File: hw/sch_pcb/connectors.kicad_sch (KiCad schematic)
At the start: 8 parts, among them J2 3.3-5V, J3 JUMP_5X2, J4 JUMP_5X2, U1 TXS0104EPW, U3 TXS0104EPW

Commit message: Update project workflows.
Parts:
- J2: symbol MLAB_Jumpers:JUMP_3X2 -> MLAB_HEADER:HEADER_2x03_PARALLEL
- J3, J4: symbol MLAB_Jumpers:JUMP_5X2 -> MLAB_HEADER:HEADER_2x04_PARALLEL
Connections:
- net at J3.1, J3.2: now also U3.10 (B4)
- net at J3.3, J3.4: now also U3.11 (B3); no longer U3.10 (B4)
- net at J3.5, J3.6: now also U3.12 (B2); no longer U3.11 (B3)
- net at J3.7, J3.8: now also U3.13 (B1); no longer U3.12 (B2)
- net at J4.1, J4.2: now also U1.10 (B4)
- net at J4.3, J4.4: now also U1.11 (B3); no longer U1.10 (B4)
- net at J4.5, J4.6: now also U1.12 (B2); no longer U1.11 (B3)
- net at J4.7, J4.8: now also U1.13 (B1); no longer U1.12 (B2)
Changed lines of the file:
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@@
 	)
 	(symbol
-		(lib_id "MLAB_Jumpers:JUMP_5X2")
-		(at 46.99 85.09 180)
+		(lib_id "MLAB_HEADER:HEADER_2x04_PARALLEL")
+		(at 50.8 82.55 180)
 		(unit 1)
 		(exclude_from_sim no)
@@
 		(fields_autoplaced yes)
 		(property "Reference" "J3"
-			(at 49.53 73.66 0)
+			(at 50.8 73.0439 0)
 			(effects
 				(font
@@
 		)
 		(property "Value" "JUMP_5X2"
-			(at 48.26 83.82 90)
+			(at 52.07 81.28 90)
 			(effects
 				(font
@@
 		)
 		(property "Footprint" "Mlab_Pin_Headers:Straight_2x05"
-			(at 49.53 76.2 0)
-			(effects
-				(font
-					(size 1.524 1.524)
-				)
+			(at 50.8 75.6725 0)
+			(effects
+				(font
+					(size 1.524 1.524)
+				)
+				(hide yes)
 			)
 		)
 		(property "Datasheet" ""
-			(at 46.99 85.09 0)
-			(effects
-				(font
-					(size 1.524 1.524)
-				)
-			)
-		)
-		(property "Description" "MLAB modified doubled pinheader connector"
-			(at 46.99 85.09 0)
-			(effects
-				(font
-					(size 1.27 1.27)
-				)
-				(hide yes)
-			)
-		)
-		(pin "9"
+			(at 50.8 86.36 0)
+			(effects
+				(font
+					(size 1.524 1.524)
+				)
+			)
+		)
+		(property "Description" "2x04 2.54 mm pitch header, 2 pins next to each other are connected"
+			(at 50.8 82.55 0)
+			(effects
+				(font
+					(size 1.27 1.27)
+				)
+				(hide yes)
+			)
+		)
+		(property "UST_ID" ""
+			(at 50.8 82.55 0)
+			(effects
+				(font
+					(size 1.27 1.27)
+				)
+				(hide yes)
+			)
 		)
 		(pin "3"
@@
 		)
 		(pin "7"
-		)
-		(pin "10"
 		)
 		(instances
@@
 	)
 	(symbol
-		(lib_id "MLAB_Jumpers:JUMP_5X2")
-		(at 46.99 132.08 180)
+		(lib_id "MLAB_HEADER:HEADER_2x04_PARALLEL")
+		(at 50.8 129.54 180)
 		(unit 1)
 		(exclude_from_sim no)
@@
 		(fields_autoplaced yes)
 		(property "Reference" "J4"
-			(at 49.53 120.65 0)
+			(at 50.8 120.0339 0)
 			(effects
 				(font
@@
 		)
 		(property "Value" "JUMP_5X2"
-			(at 48.26 130.81 90)
+			(at 52.07 128.27 90)
 			(effects
 				(font
@@
 		)
 		(property "Footprint" "Mlab_Pin_Headers:Straight_2x05"
-			(at 49.53 123.19 0)
-			(effects
-				(font
-					(size 1.524 1.524)
-				)
+			(at 50.8 122.6625 0)
+			(effects
+				(font
+					(size 1.524 1.524)
+				)
+				(hide yes)
 			)
 		)
 		(property "Datasheet" ""
-			(at 46.99 132.08 0)
-			(effects
-				(font
-					(size 1.524 1.524)
-				)
-			)
-		)
-		(property "Description" "MLAB modified doubled pinheader connector"
-			(at 46.99 132.08 0)
-			(effects
-				(font
-					(size 1.27 1.27)
-				)
-				(hide yes)
-			)
-		)
-		(pin "9"
+			(at 50.8 133.35 0)
+			(effects
+				(font
+					(size 1.524 1.524)
+				)
+			)
+		)
+		(property "Description" "2x04 2.54 mm pitch header, 2 pins next to each other are connected"
+			(at 50.8 129.54 0)
+			(effects
+				(font
+					(size 1.27 1.27)
+				)
+				(hide yes)
+			)
+		)
+		(property "UST_ID" ""
+			(at 50.8 129.54 0)
+			(effects
+				(font
+					(size 1.27 1.27)
+				)
+				(hide yes)
+			)
 		)
 		(pin "3"
@@
 		)
 		(pin "7"
-		)
-		(pin "10"
 		)
 		(instances
@@
 	)
 	(symbol
-		(lib_id "MLAB_Jumpers:JUMP_3X2")
-		(at 45.72 39.37 0)
+		(lib_id "MLAB_HEADER:HEADER_2x03_PARALLEL")
+		(at 49.53 38.1 0)
 		(mirror y)
 		(unit 1)
@@
 		(dnp no)
 		(property "Reference" "J2"
-			(at 47.498 42.418 0)
+			(at 51.308 41.148 0)
 			(effects
 				(font
@@
 		)
 		(property "Value" "3.3-5V"
-			(at 49.022 32.766 0)
+			(at 52.832 31.496 0)
 			(effects
 				(font
@@
 		)
 		(property "Footprint" "Mlab_Pin_Headers:Straight_2x03"
-			(at 45.72 39.37 0)
+			(at 49.53 35.56 0)
 			(effects
 				(font
@@
 		)
 		(property "Datasheet" ""
-			(at 45.72 39.37 0)
-			(effects
-				(font
-					(size 1.524 1.524)
-				)
-			)
-		)
-		(property "Description" "MLAB modified doubled pinheader connector"
-			(at 45.72 39.37 0)
-			(effects
-				(font
+			(at 49.53 35.56 0)
+			(effects
+				(font
+					(size 1.524 1.524)
+				)
+			)
+		)
+		(property "Description" "2x03 2.54 mm pitch header, 2 pins next to each other are connected"
+			(at 49.53 38.1 0)
+			(effects
+				(font
+					(size 1.27 1.27)
+				)
+				(hide yes)
+			)
+		)
+		(property "UST_ID" ""
+			(at 49.53 38.1 0)
+			(effects
+				(font

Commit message: Fix footprint of pin-headers.
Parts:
- J3, J4: footprint Mlab_Pin_Headers:Straight_2x05 -> Mlab_Pin_Headers:Straight_2x04
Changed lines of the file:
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@@
 			)
 		)
-		(property "Footprint" "Mlab_Pin_Headers:Straight_2x05"
+		(property "Footprint" "Mlab_Pin_Headers:Straight_2x04"
 			(at 50.8 75.6725 0)
 			(effects
@@
 			)
 		)
-		(property "Footprint" "Mlab_Pin_Headers:Straight_2x05"
+		(property "Footprint" "Mlab_Pin_Headers:Straight_2x04"
 			(at 50.8 122.6625 0)
 			(effects

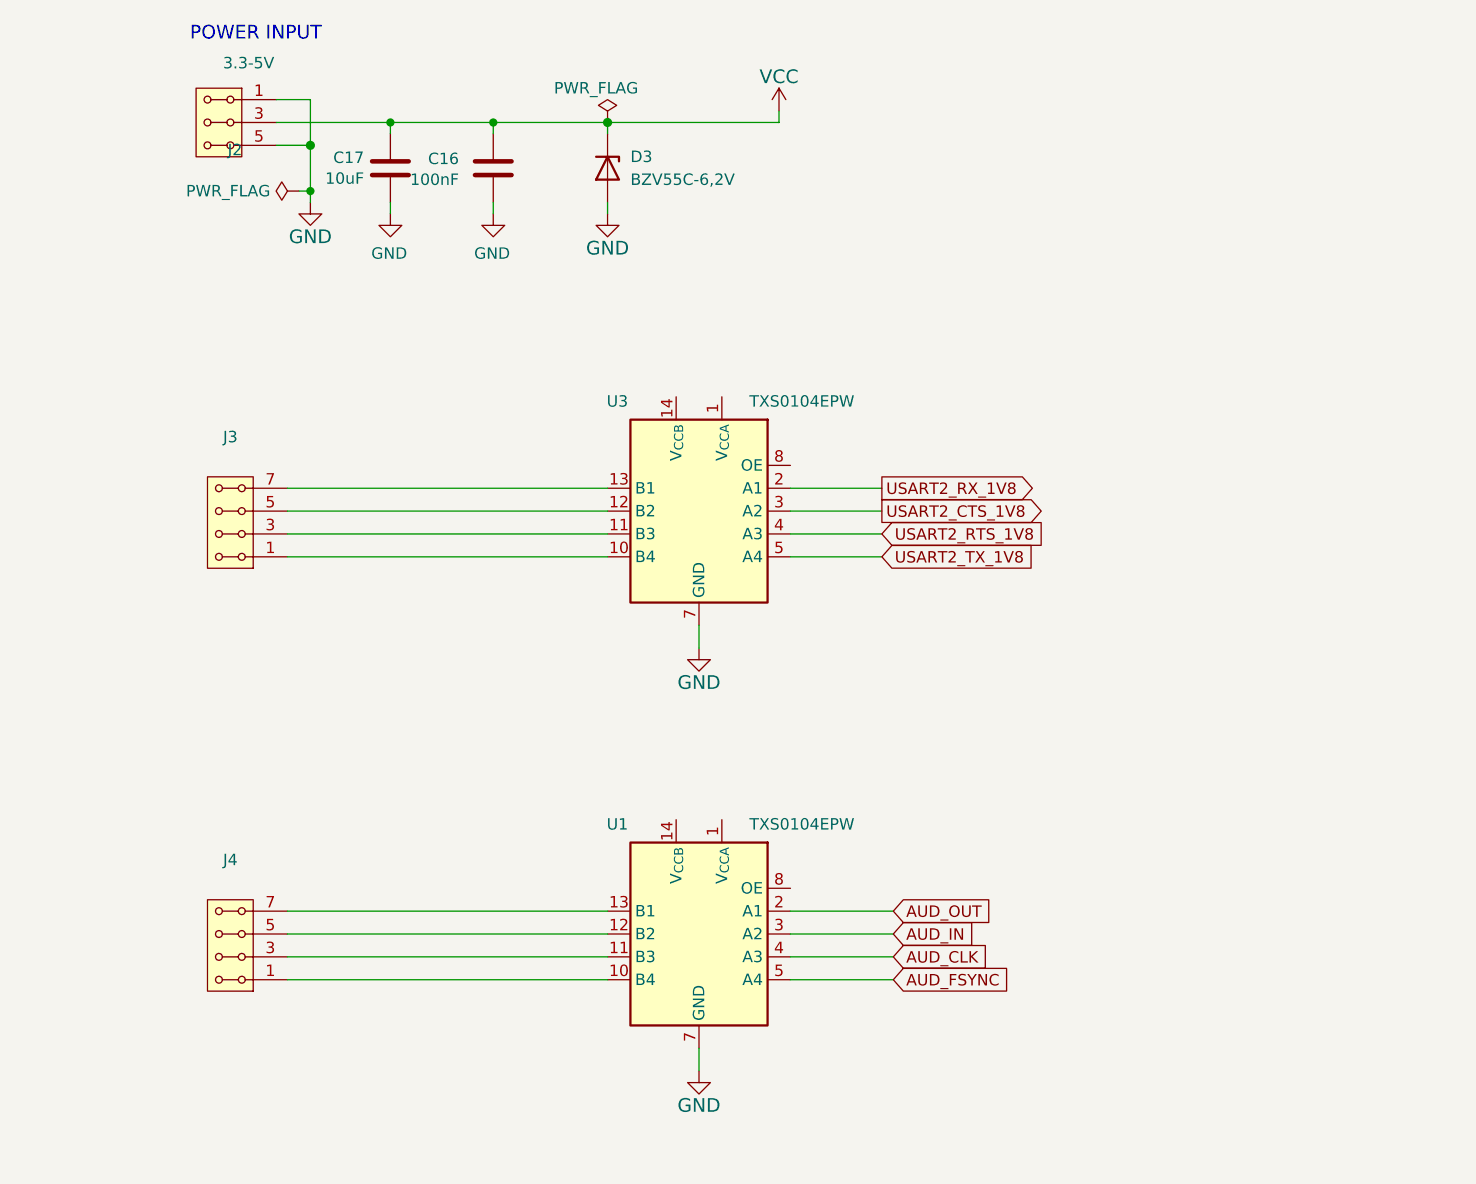
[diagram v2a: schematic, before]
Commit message: Add text for connectors
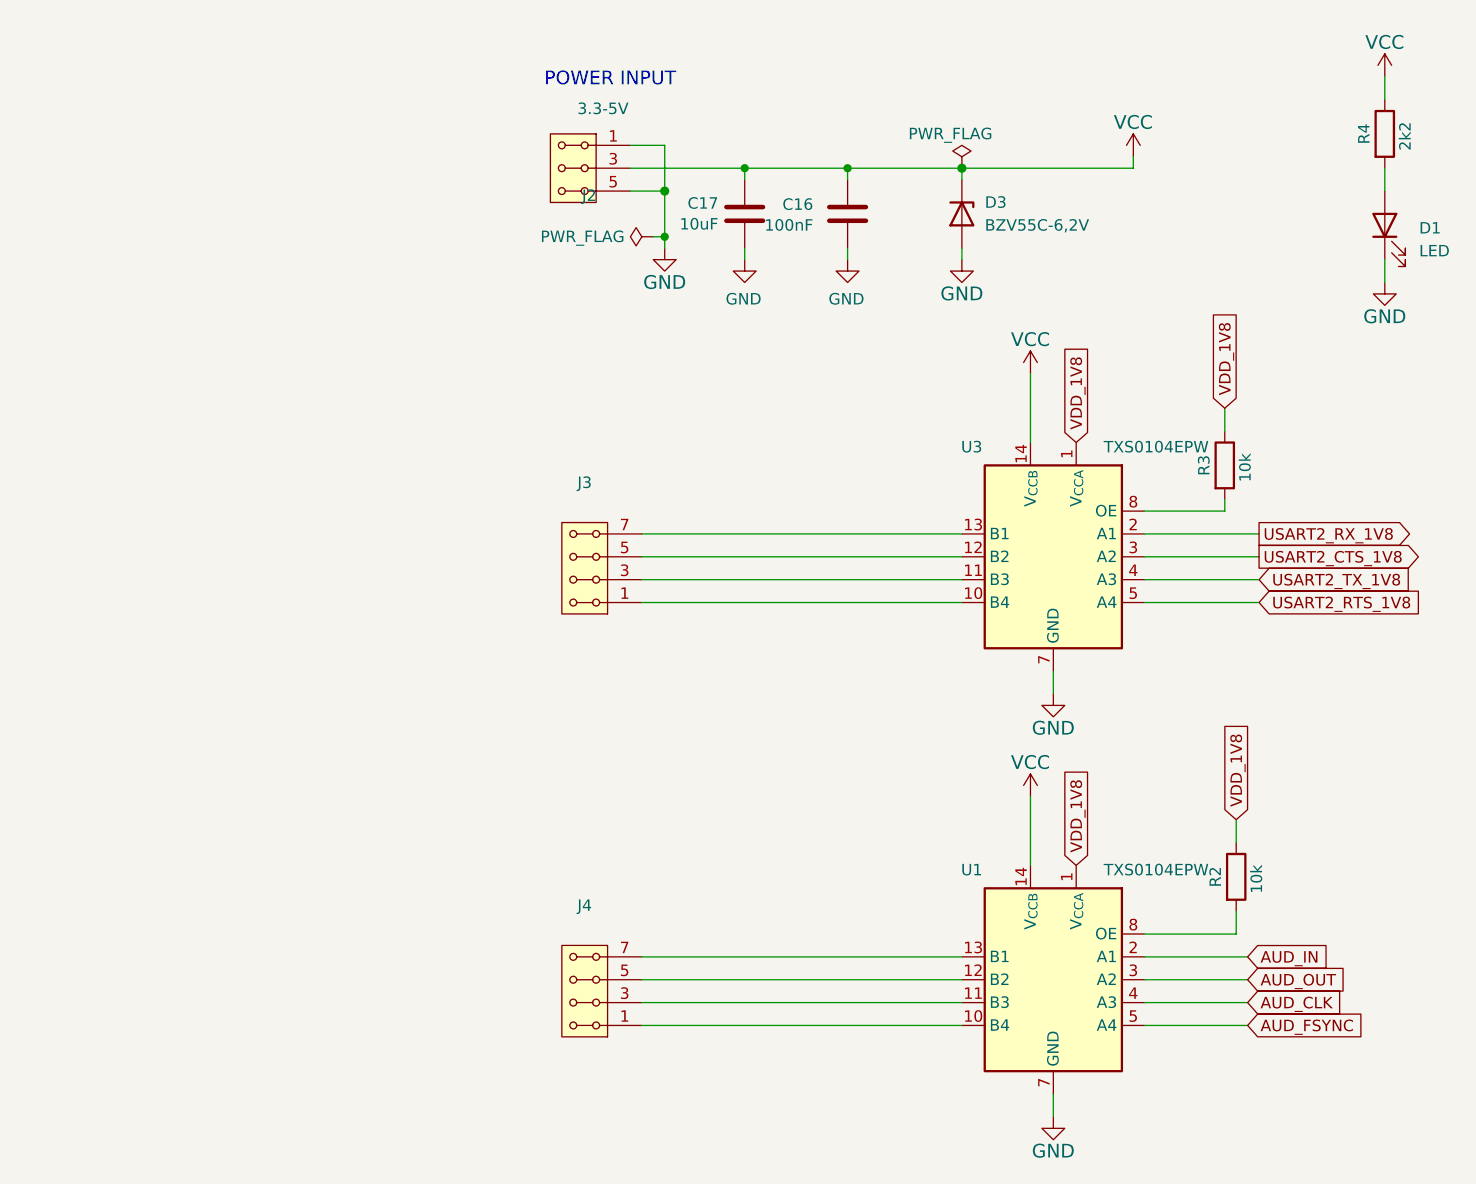
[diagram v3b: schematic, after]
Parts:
- added D1: LED, LED_SMD:LED_0805_2012Metric, symbol Device:LED
- added R2, R3: 10k, Resistor_SMD:R_0603_1608Metric, symbol cc2564-board-rescue:R-Device
- added R4: 2k2, Resistor_SMD:R_0603_1608Metric, symbol cc2564-board-rescue:R-Device
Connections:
- net AUD_IN: now also U1.2 (A1); no longer U1.3 (A2)
- net AUD_OUT: now also U1.3 (A2); no longer U1.2 (A1)
- net GND: now also D1.1 (K)
- net USART2_RTS_1V8: now also U3.5 (A4); no longer U3.4 (A3)
- net USART2_TX_1V8: now also U3.4 (A3); no longer U3.5 (A4)
- net VCC: now also U1.14 (V_{CCB}), U3.14 (V_{CCB}), R4.1
- net VDD_1V8: now reaches U1.1 (V_{CCA})
- net VDD_1V8: now also U3.1 (V_{CCA}), R2.1, R3.1
- net at U1.8 (OE): now also R2.2
- net at U3.8 (OE): now also R3.2
- new net: D1.2 (A), R4.2
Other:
- moved on the sheet: C16, C17, D3, J2, J3, J4, U1, U3

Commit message: Cleanup layout. Fix obsolete part types.
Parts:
- D1: footprint LED_SMD:LED_0805_2012Metric -> Mlab_D:LED_1206_mill
- D3: value BZV55C-6,2V -> BZX585-B5V6.115; footprint Diode_SMD:D_MiniMELF -> Diode_SMD:D_SOD-523; UST_ID 604b0326128750769e5b0f93 -> 60879d38128750769ee58e48
- J2: value 3.3-5V -> 3.3V
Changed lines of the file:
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@@
 		(dnp no)
 		(property "Reference" "C16"
-			(at 115.57 47.2186 0)
+			(at 125.73 45.72 0)
 			(effects
 				(font
@@
 		)
 		(property "Value" "100nF"
-			(at 115.57 49.53 0)
+			(at 127 50.8 0)
 			(effects
 				(font
@@
 			)
 		)
-		(property "Footprint" "LED_SMD:LED_0805_2012Metric"
+		(property "Footprint" "Mlab_D:LED_1206_mill"
 			(at 179.07 49.53 0)
 			(effects
@@
 			)
 		)
+		(property "UST_ID" ""
+			(at 179.07 49.53 0)
+			(effects
+				(font
+					(size 1.27 1.27)
+				)
+				(hide yes)
+			)
+		)
 		(pin "2"
 		)
@@
 			)
 		)
-		(property "Value" "BZV55C-6,2V"
+		(property "Value" "BZX585-B5V6.115"
 			(at 134.62 49.5299 90)
 			(effects
@@
 			)
 		)
-		(property "Footprint" "Diode_SMD:D_MiniMELF"
+		(property "Footprint" "Diode_SMD:D_SOD-523"
 			(at 132.08 48.26 0)
 			(effects
@@
 			)
 		)
-		(property "Datasheet" "~"
+		(property "Datasheet" "https://www.tme.eu/Document/7f59fc987b8fce7e4ab18399d6e66bd1/BZX585-DTE.pdf"
 			(at 132.08 48.26 0)
 			(effects
@@
 			)
 		)
-		(property "UST_ID" "604b0326128750769e5b0f93"
+		(property "UST_ID" "60879d38128750769ee58e48"
 			(at 132.08 48.26 0)
 			(effects
@@
 		(dnp no)
 		(property "Reference" "J2"
-			(at 90.678 46.228 0)
-			(effects
-				(font
-					(size 1.27 1.27)
-				)
-			)
-		)
-		(property "Value" "3.3-5V"
+			(at 83.82 43.18 0)
+			(effects
+				(font
+					(size 1.27 1.27)
+				)
+			)
+		)
+		(property "Value" "3.3V"
 			(at 92.202 36.576 0)
 			(effects

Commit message: Update UST_IDs.
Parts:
- C16: UST_ID 5c70984712875079b91f8b4c -> 5c70984812875079b91f8bf2
- D1: UST_ID (none) -> 64ab2ec176c82a1d3b57875b
- R2, R3: UST_ID (none) -> 5c70984512875079b91f8962
- R4: UST_ID (none) -> 5c70984512875079b91f895e
- U1, U3: UST_ID (none) -> 6998b3d2d42e6e3c4d330d92
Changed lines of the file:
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@@
+			)
+		)
+		(property "UST_ID" "5c70984512875079b91f895e"
+			(at 179.07 39.37 90)
+			(effects
+				(font
+					(size 1.27 1.27)
+				)
+				(hide yes)
 			)
 		)
@@
 			)
 		)
-		(property "UST_ID" "5c70984712875079b91f8b4c"
+		(property "UST_ID" "5c70984812875079b91f8bf2"
 			(at 119.38 48.26 0)
 			(effects
@@
 					(size 1.27 1.27)
 				)
+			)
+		)
+		(property "UST_ID" "5c70984512875079b91f8962"
+			(at 161.29 76.2 90)
+			(effects
+				(font
+					(size 1.27 1.27)
+				)
+				(hide yes)
 			)
 		)
@@
 			)
 		)
-		(property "UST_ID" ""
+		(property "UST_ID" "64ab2ec176c82a1d3b57875b"
 			(at 179.07 49.53 0)
 			(effects
@@
 			)
 		)
+		(property "UST_ID" "6998b3d2d42e6e3c4d330d92"
+			(at 142.24 133.35 0)
+			(effects
+				(font
+					(size 1.27 1.27)
+				)
+				(hide yes)
+			)
+		)
 		(pin "8"
 		)
@@
 			)
 		)
+		(property "UST_ID" "6998b3d2d42e6e3c4d330d92"
+			(at 142.24 86.36 0)
+			(effects
+				(font
+					(size 1.27 1.27)
+				)
+				(hide yes)
+			)
+		)
 		(pin "8"
 		)
@@
 			)
 		)
+		(property "UST_ID" "5c70984512875079b91f8962"
+			(at 162.56 121.92 90)
+			(effects
+				(font
+					(size 1.27 1.27)
+				)
+				(hide yes)
+			)
+		)
